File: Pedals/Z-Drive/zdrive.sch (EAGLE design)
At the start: 26 parts, among them IC1 MC1458P, Q1 2N7000, Q2 2N7000

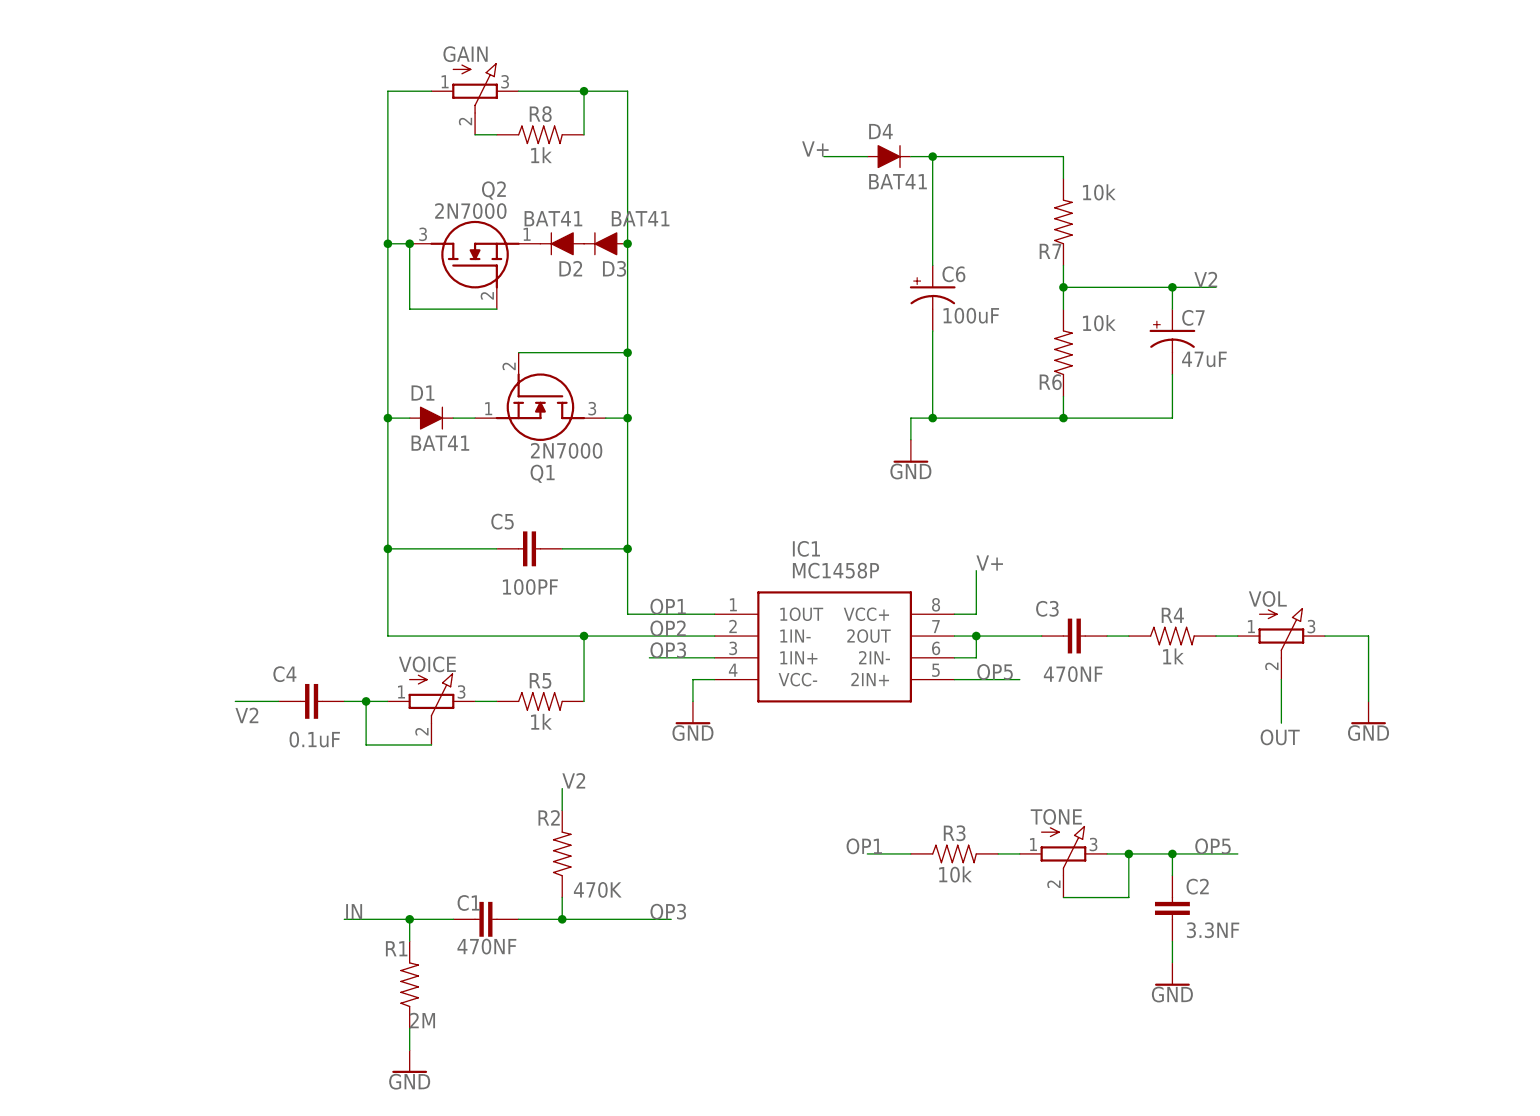
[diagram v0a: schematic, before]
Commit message: Update zdrive schematic with new pots
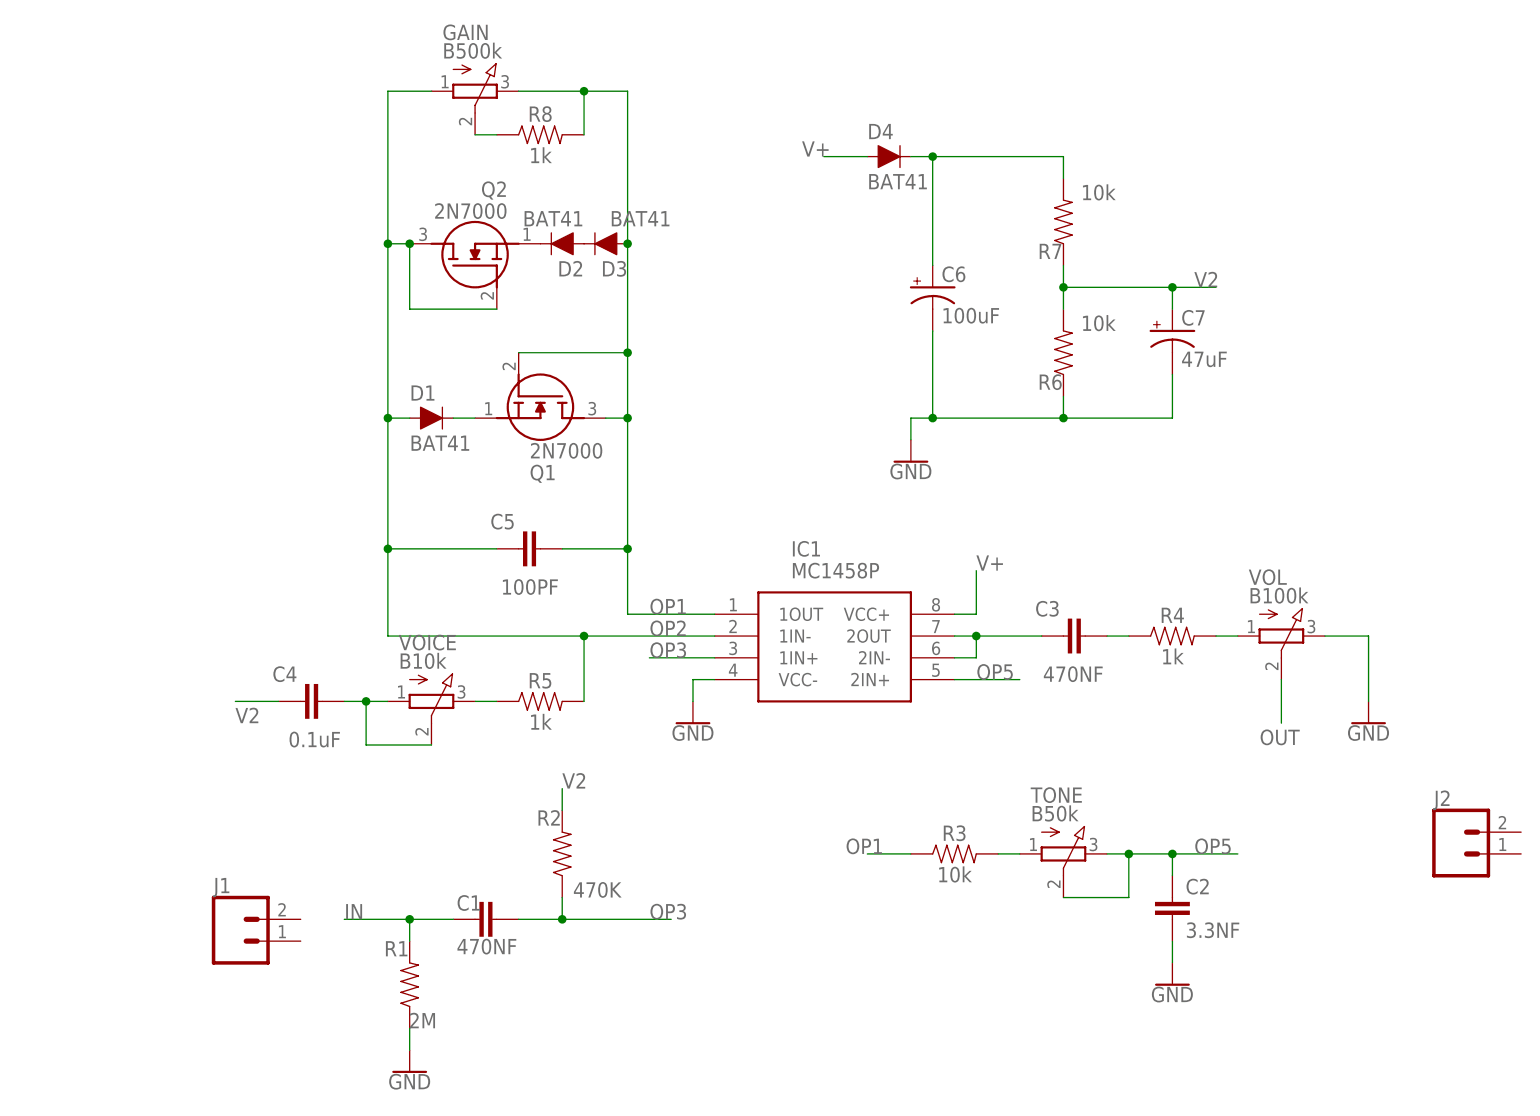
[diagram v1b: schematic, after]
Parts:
- added J1, J2: (no value), SparkFun-Connectors:CONN_02
- GAIN: value (none) -> B500k; device pot:3RP/1610N -> Custom-Parts:16MMPOT
- TONE: value (none) -> B50k; device pot:3RP/1610N -> Custom-Parts:16MMPOT
- VOICE: value (none) -> B10k; device pot:3RP/1610N -> Custom-Parts:16MMPOT
- VOL: value (none) -> B100k; device pot:3RP/1610N -> Custom-Parts:16MMPOT

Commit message: Update schematic and begin board layout
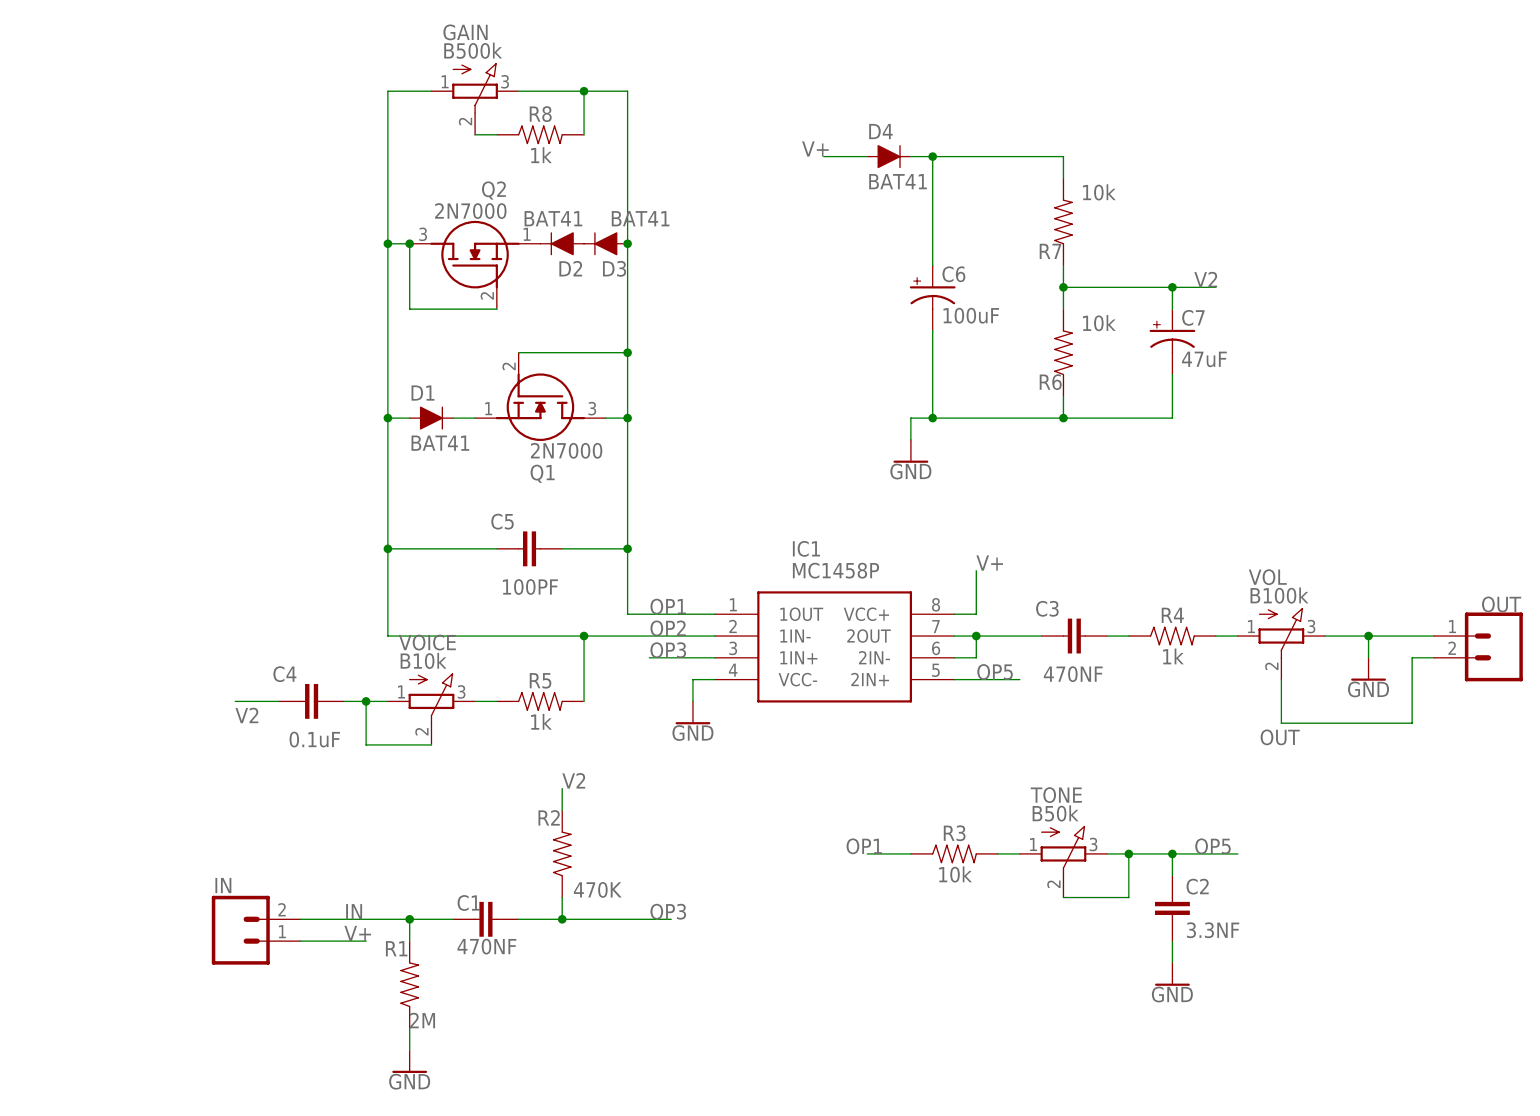
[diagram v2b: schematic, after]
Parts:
- removed J2: (no value), SparkFun-Connectors:CONN_02
- added OUT: (no value), SparkFun-Connectors:CONN_02
- renumbered J1 to IN
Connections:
- net GND: now also OUT.1
- net IN: now also IN.2
- net OUT: now also OUT.2
- net V+: now also IN.1
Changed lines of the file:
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@@
 <part name="TONE" library="Custom-Parts" deviceset="16MMPOT" device="" package3d_urn="urn:adsk.eagle:package:22726/1" value="B50k"/>
 <part name="VOL" library="Custom-Parts" deviceset="16MMPOT" device="" package3d_urn="urn:adsk.eagle:package:22726/1" value="B100k"/>
-<part name="J1" library="SparkFun-Connectors" library_urn="urn:adsk.eagle:library:513" deviceset="CONN_02" device="" package3d_urn="urn:adsk.eagle:package:38039/1"/>
-<part name="J2" library="SparkFun-Connectors" library_urn="urn:adsk.eagle:library:513" deviceset="CONN_02" device="" package3d_urn="urn:adsk.eagle:package:38039/1"/>
+<part name="IN" library="SparkFun-Connectors" library_urn="urn:adsk.eagle:library:513" deviceset="CONN_02" device="" package3d_urn="urn:adsk.eagle:package:38039/1"/>
+<part name="OUT" library="SparkFun-Connectors" library_urn="urn:adsk.eagle:library:513" deviceset="CONN_02" device="" package3d_urn="urn:adsk.eagle:package:38039/1"/>
 </parts>
 <sheets>
@@
 <attribute name="VALUE" x="73.66" y="79.756" size="1.778" layer="96" font="vector" align="top-center"/>
 </instance>
-<instance part="GND4" gate="1" x="96.52" y="71.12" smashed="yes">
-<attribute name="VALUE" x="96.52" y="70.866" size="1.778" layer="96" align="top-center"/>
+<instance part="GND4" gate="1" x="96.52" y="76.2" smashed="yes">
+<attribute name="VALUE" x="96.52" y="75.946" size="1.778" layer="96" align="top-center"/>
 </instance>
 <instance part="R5" gate="G$1" x="0" y="73.66" smashed="yes">
@@
 <attribute name="VALUE" x="82.55" y="85.09" size="1.778" layer="96"/>
 </instance>
-<instance part="J1" gate="G$1" x="-35.56" y="45.72" smashed="yes">
+<instance part="IN" gate="G$1" x="-35.56" y="45.72" smashed="yes">
 <attribute name="VALUE" x="-38.1" y="40.894" size="1.778" layer="96" font="vector"/>
 <attribute name="NAME" x="-38.1" y="51.308" size="1.778" layer="95" font="vector"/>
 </instance>
-<instance part="J2" gate="G$1" x="106.68" y="55.88" smashed="yes">
-<attribute name="VALUE" x="104.14" y="51.054" size="1.778" layer="96" font="vector"/>
-<attribute name="NAME" x="104.14" y="61.468" size="1.778" layer="95" font="vector"/>
+<instance part="OUT" gate="G$1" x="111.76" y="81.28" smashed="yes" rot="R180">
+<attribute name="VALUE" x="114.3" y="86.106" size="1.778" layer="96" font="vector" rot="R180"/>
+<attribute name="NAME" x="114.3" y="85.852" size="1.778" layer="95" font="vector" rot="R180"/>
 </instance>
 </instances>
@@
 <wire x1="91.44" y1="81.28" x2="96.52" y2="81.28" width="0.1524" layer="91"/>
 <pinref part="GND4" gate="1" pin="GND"/>
-<wire x1="96.52" y1="81.28" x2="96.52" y2="73.66" width="0.1524" layer="91"/>
+<wire x1="96.52" y1="81.28" x2="96.52" y2="78.74" width="0.1524" layer="91"/>
 <pinref part="VOL" gate="G$1" pin="E"/>
+<pinref part="OUT" gate="G$1" pin="1"/>
+<wire x1="96.52" y1="81.28" x2="104.14" y2="81.28" width="0.1524" layer="91"/>
+<junction x="96.52" y="81.28"/>
 </segment>
 </net>
@@
 <pinref part="C1" gate="G$1" pin="2"/>
 <wire x1="-15.24" y1="48.26" x2="-10.16" y2="48.26" width="0.1524" layer="91"/>
-<wire x1="-15.24" y1="48.26" x2="-22.86" y2="48.26" width="0.1524" layer="91"/>
+<wire x1="-15.24" y1="48.26" x2="-27.94" y2="48.26" width="0.1524" layer="91"/>
 <junction x="-15.24" y="48.26"/>
 <label x="-22.86" y="48.26" size="1.778" layer="95"/>
+<pinref part="IN" gate="G$1" pin="2"/>
 </segment>
 </net>
@@
 <wire x1="38.1" y1="137.16" x2="33.02" y2="137.16" width="0.1524" layer="91"/>
 <label x="30.48" y="137.16" size="1.778" layer="95"/>
+</segment>
+<segment>
+<pinref part="IN" gate="G$1" pin="1"/>
+<wire x1="-27.94" y1="45.72" x2="-20.32" y2="45.72" width="0.1524" layer="91"/>
+<label x="-22.86" y="45.72" size="1.778" layer="95"/>
 </segment>
 </net>
@@
 <label x="83.82" y="68.58" size="1.778" layer="95"/>
 <pinref part="VOL" gate="G$1" pin="S"/>
-</segment>
-</net>
+<wire x1="86.36" y1="71.12" x2="101.6" y2="71.12" width="0.1524" layer="91"/>
+<wire x1="101.6" y1="71.12" x2="101.6" y2="78.74" width="0.1524" layer="91"/>
+<pinref part="OUT" gate="G$1" pin="2"/>
+<wire x1="101.6" y1="78.74" x2="104.14" y2="78.74" width="0.1524" layer="91"/>
+</segment>
+</net>

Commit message: Working on layout
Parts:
- removed D4: BAT41, SparkFun-DiscreteSemi:DIODE-KIT2
- added D5: BAT41, SparkFun-DiscreteSemi:DIODE-KIT2
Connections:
- new net 9V: D5.A, IN.1
- net V+: now also D5.C; no longer D4.A, D4.C, IN.1
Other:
- moved on the sheet: IN
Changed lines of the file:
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@@
 <part name="R8" library="SparkFun-Resistors" library_urn="urn:adsk.eagle:library:532" deviceset="1KOHM" device="-HORIZ-1/4W-5%" package3d_urn="urn:adsk.eagle:package:39658/1" value="1k"/>
 <part name="Q1" library="SamacSys_Parts" deviceset="2N7000" device=""/>
-<part name="D4" library="SparkFun-DiscreteSemi" library_urn="urn:adsk.eagle:library:514" deviceset="DIODE" device="-KIT2" package3d_urn="urn:adsk.eagle:package:38455/1" value="BAT41"/>
 <part name="GAIN" library="Custom-Parts" deviceset="16MMPOT" device="" package3d_urn="urn:adsk.eagle:package:22726/1" value="B500k"/>
 <part name="VOICE" library="Custom-Parts" deviceset="16MMPOT" device="" package3d_urn="urn:adsk.eagle:package:22726/1" value="B10k"/>
@@
 <part name="IN" library="SparkFun-Connectors" library_urn="urn:adsk.eagle:library:513" deviceset="CONN_02" device="" package3d_urn="urn:adsk.eagle:package:38039/1"/>
 <part name="OUT" library="SparkFun-Connectors" library_urn="urn:adsk.eagle:library:513" deviceset="CONN_02" device="" package3d_urn="urn:adsk.eagle:package:38039/1"/>
+<part name="D5" library="SparkFun-DiscreteSemi" library_urn="urn:adsk.eagle:library:514" deviceset="DIODE" device="-KIT2" package3d_urn="urn:adsk.eagle:package:38455/1" value="BAT41"/>
 </parts>
 <sheets>
@@
 <attribute name="VALUE" x="-1.27" y="102.87" size="1.778" layer="96" align="center-left"/>
 </instance>
-<instance part="D4" gate="G$1" x="40.64" y="137.16" smashed="yes">
-<attribute name="NAME" x="38.1" y="139.192" size="1.778" layer="95" font="vector"/>
-<attribute name="VALUE" x="38.1" y="135.128" size="1.778" layer="96" font="vector" align="top-left"/>
-</instance>
 <instance part="GAIN" gate="G$1" x="-7.62" y="144.78" smashed="yes" rot="R270">
 <attribute name="NAME" x="-11.43" y="150.749" size="1.778" layer="95"/>
@@
 <attribute name="VALUE" x="82.55" y="85.09" size="1.778" layer="96"/>
 </instance>
-<instance part="IN" gate="G$1" x="-35.56" y="45.72" smashed="yes">
-<attribute name="VALUE" x="-38.1" y="40.894" size="1.778" layer="96" font="vector"/>
-<attribute name="NAME" x="-38.1" y="51.308" size="1.778" layer="95" font="vector"/>
+<instance part="IN" gate="G$1" x="-40.64" y="45.72" smashed="yes">
+<attribute name="VALUE" x="-43.18" y="40.894" size="1.778" layer="96" font="vector"/>
+<attribute name="NAME" x="-43.18" y="51.308" size="1.778" layer="95" font="vector"/>
 </instance>
 <instance part="OUT" gate="G$1" x="111.76" y="81.28" smashed="yes" rot="R180">
 <attribute name="VALUE" x="114.3" y="86.106" size="1.778" layer="96" font="vector" rot="R180"/>
 <attribute name="NAME" x="114.3" y="85.852" size="1.778" layer="95" font="vector" rot="R180"/>
+</instance>
+<instance part="D5" gate="G$1" x="-25.4" y="43.18" smashed="yes">
+<attribute name="NAME" x="-27.94" y="45.212" size="1.778" layer="95" font="vector"/>
+<attribute name="VALUE" x="-27.94" y="41.148" size="1.778" layer="96" font="vector" align="top-left"/>
 </instance>
 </instances>
@@
 <pinref part="C1" gate="G$1" pin="2"/>
 <wire x1="-15.24" y1="48.26" x2="-10.16" y2="48.26" width="0.1524" layer="91"/>
-<wire x1="-15.24" y1="48.26" x2="-27.94" y2="48.26" width="0.1524" layer="91"/>
+<wire x1="-15.24" y1="48.26" x2="-33.02" y2="48.26" width="0.1524" layer="91"/>
 <junction x="-15.24" y="48.26"/>
 <label x="-22.86" y="48.26" size="1.778" layer="95"/>
@@
 </segment>
 <segment>
+<label x="30.48" y="137.16" size="1.778" layer="95"/>
 <pinref part="C6" gate="G$1" pin="+"/>
 <wire x1="45.72" y1="124.46" x2="45.72" y2="137.16" width="0.1524" layer="91"/>
@@
 <wire x1="60.96" y1="134.62" x2="60.96" y2="137.16" width="0.1524" layer="91"/>
 <wire x1="60.96" y1="137.16" x2="45.72" y2="137.16" width="0.1524" layer="91"/>
-<pinref part="D4" gate="G$1" pin="C"/>
-<wire x1="45.72" y1="137.16" x2="43.18" y2="137.16" width="0.1524" layer="91"/>
 <junction x="45.72" y="137.16"/>
-</segment>
-<segment>
-<pinref part="D4" gate="G$1" pin="A"/>
-<wire x1="38.1" y1="137.16" x2="33.02" y2="137.16" width="0.1524" layer="91"/>
-<label x="30.48" y="137.16" size="1.778" layer="95"/>
-</segment>
-<segment>
-<pinref part="IN" gate="G$1" pin="1"/>
-<wire x1="-27.94" y1="45.72" x2="-20.32" y2="45.72" width="0.1524" layer="91"/>
-<label x="-22.86" y="45.72" size="1.778" layer="95"/>
+<wire x1="33.02" y1="137.16" x2="45.72" y2="137.16" width="0.1524" layer="91"/>
+</segment>
+<segment>
+<pinref part="D5" gate="G$1" pin="C"/>
+<wire x1="-22.86" y1="43.18" x2="-20.32" y2="43.18" width="0.1524" layer="91"/>
+<label x="-22.86" y="43.18" size="1.778" layer="95"/>
 </segment>
 </net>
@@
 </segment>
 </net>
+<net name="9V" class="0">
+<segment>
+<pinref part="IN" gate="G$1" pin="1"/>
+<wire x1="-33.02" y1="45.72" x2="-30.48" y2="45.72" width="0.1524" layer="91"/>
+<wire x1="-30.48" y1="45.72" x2="-30.48" y2="43.18" width="0.1524" layer="91"/>
+<pinref part="D5" gate="G$1" pin="A"/>
+<wire x1="-30.48" y1="43.18" x2="-27.94" y2="43.18" width="0.1524" layer="91"/>
+</segment>
+</net>
